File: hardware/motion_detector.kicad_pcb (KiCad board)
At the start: 2 copper layers, 45 x 25 mm, 16 parts, among them P1 CON-SENSOR, U1 M24C64, U2 HC-SR501, U3 DRILL, U4 DRILL, U5 DRILL, U6 DRILL

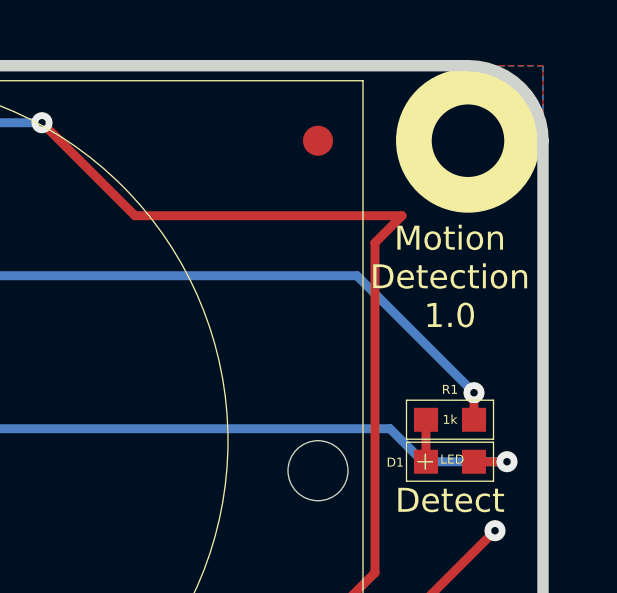
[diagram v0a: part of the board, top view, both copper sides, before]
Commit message: fix pcb name
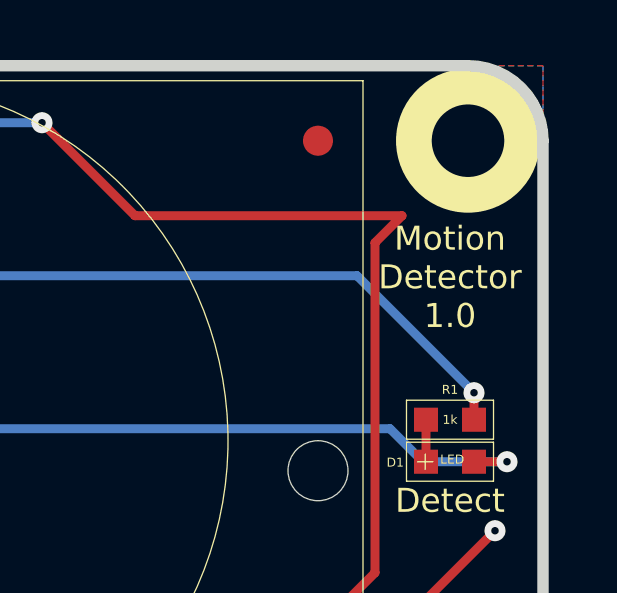
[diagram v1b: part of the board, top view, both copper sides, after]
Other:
- board text added: "Motion Detector 1.0"
- board text removed: "Motion Detection 1.0"
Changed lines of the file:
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@@
   (gr_line (start 45.4 29.8) (end 85.3 29.8) (angle 90) (layer Edge.Cuts) (width 0.381))
   (gr_line (start 45.4 54.8) (end 85.3 54.8) (angle 90) (layer Edge.Cuts) (width 0.381))
-  (gr_text "Motion\nDetection\n1.0" (at 84.8 36.85) (layer F.SilkS)
+  (gr_text "Motion\nDetector\n1.0" (at 84.8 36.85) (layer F.SilkS)
     (effects (font (size 0.8 0.8) (thickness 0.15)))
   )
